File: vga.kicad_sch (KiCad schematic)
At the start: 52 parts

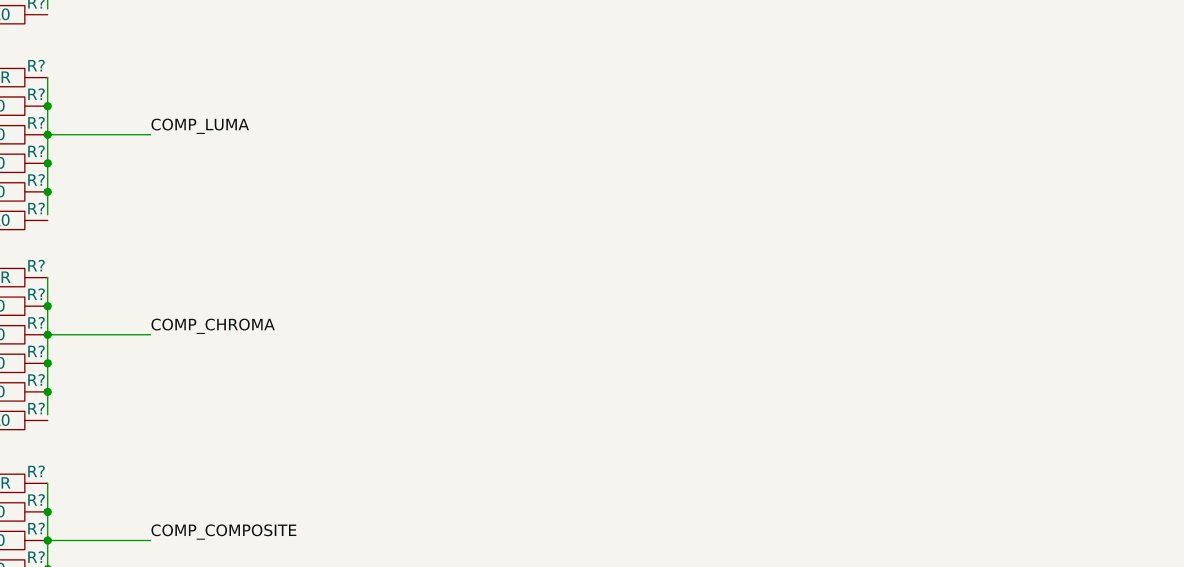
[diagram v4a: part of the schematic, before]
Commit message: add 3.5mm audio jack
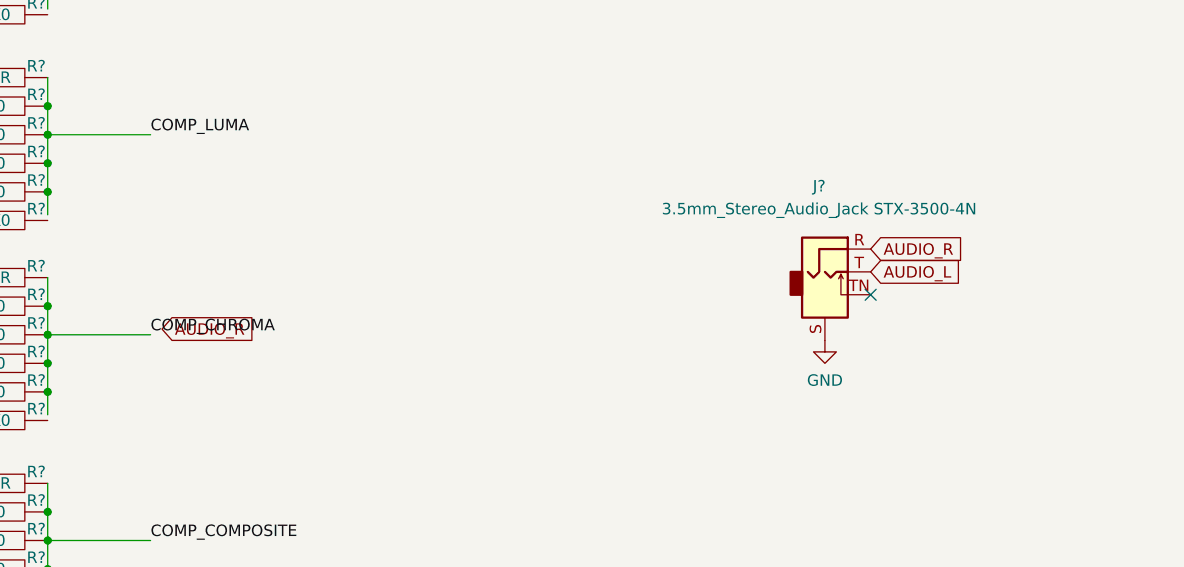
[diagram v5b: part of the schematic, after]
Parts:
- added J?: 3.5mm_Stereo_Audio_Jack STX-3500-4N, Connector_Audio:Jack_3.5mm_CUI_SJ-3524-SMT_Horizontal, symbol 00Project-SDF-60J:3.5mm_Stereo_Audio_Jack STX-3500-4N
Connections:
- net AUDIO_L: now also J?.T
- net AUDIO_R: now also J?.R
- net GND: now also J?.S
- no-connect marks 5 -> 6
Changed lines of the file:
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@@
   (no_connect (at 243.84 120.015))
   (no_connect (at 228.6 54.61))
+  (no_connect (at 139.065 132.715))
   (no_connect (at 243.84 114.935))
   (no_connect (at 228.6 52.07))
@@
     )
   )
+  (global_label "AUDIO_R" (shape input) (at 60.325 136.525 0) (fields_autoplaced)
+    (effects (font (size 1.27 1.27)) (justify left))
+    (property "Intersheet References" "${INTERSHEET_REFS}" (id 0) (at 70.6 136.4456 0)
+      (effects (font (size 1.27 1.27)) (justify left) hide)
+    )
+  )
   (global_label "AUDIO_L1" (shape input) (at 34.925 74.295 180) (fields_autoplaced)
     (effects (font (size 1.27 1.27)) (justify right))
@@
     (property "Intersheet References" "${INTERSHEET_REFS}" (id 0) (at 17.2719 140.2556 0)
       (effects (font (size 1.27 1.27)) (justify right) hide)
+    )
+  )
+  (global_label "AUDIO_R" (shape input) (at 139.065 127.635 0) (fields_autoplaced)
+    (effects (font (size 1.27 1.27)) (justify left))
+    (property "Intersheet References" "${INTERSHEET_REFS}" (id 0) (at 149.34 127.5556 0)
+      (effects (font (size 1.27 1.27)) (justify left) hide)
     )
   )
@@
     (property "Intersheet References" "${INTERSHEET_REFS}" (id 0) (at 165.9526 15.7956 0)
       (effects (font (size 1.27 1.27)) (justify right) hide)
+    )
+  )
+  (global_label "AUDIO_L" (shape input) (at 139.065 130.175 0) (fields_autoplaced)
+    (effects (font (size 1.27 1.27)) (justify left))
+    (property "Intersheet References" "${INTERSHEET_REFS}" (id 0) (at 149.0981 130.0956 0)
+      (effects (font (size 1.27 1.27)) (justify left) hide)
     )
   )
@@
     (pin "2")
   )
+  (symbol (lib_id "power:GND") (at 133.985 137.795 0) (unit 1)
+    (in_bom yes) (on_board yes) (fields_autoplaced)
+    (property "Reference" "#PWR?" (id 0) (at 133.985 144.145 0)
+      (effects (font (size 1.27 1.27)) hide)
+    )
+    (property "Value" "GND" (id 1) (at 133.985 142.24 0))
+    (property "Footprint" "" (id 2) (at 133.985 137.795 0)
+      (effects (font (size 1.27 1.27)) hide)
+    )
+    (property "Datasheet" "" (id 3) (at 133.985 137.795 0)
+      (effects (font (size 1.27 1.27)) hide)
+    )
+    (pin "1")
+  )
   (symbol (lib_id "pspice:R") (at 41.275 160.02 90) (unit 1)
     (in_bom yes) (on_board yes)
@@
     (pin "2")
   )
+  (symbol (lib_id "00Project-SDF-60J:3.5mm_Stereo_Audio_Jack STX-3500-4N") (at 133.985 130.175 0) (unit 1)
+    (in_bom yes) (on_board yes) (fields_autoplaced)
+    (property "Reference" "J?" (id 0) (at 133.35 120.65 0))
+    (property "Value" "3.5mm_Stereo_Audio_Jack STX-3500-4N" (id 1) (at 133.35 123.19 0))
+    (property "Footprint" "Connector_Audio:Jack_3.5mm_CUI_SJ-3524-SMT_Horizontal" (id 2) (at 131.445 117.475 0)
+      (effects (font (size 1.27 1.27)) hide)
+    )
+    (property "Datasheet" "https://www.kycon.com/Pub_Eng_Draw/STX-3500-4N.pdf" (id 3) (at 133.985 120.015 0)
+      (effects (font (size 1.27 1.27)) hide)
+    )
+    (pin "R")
+    (pin "S")
+    (pin "T")
+    (pin "TN")
+  )
   (symbol (lib_id "pspice:R") (at 41.275 95.25 90) (unit 1)

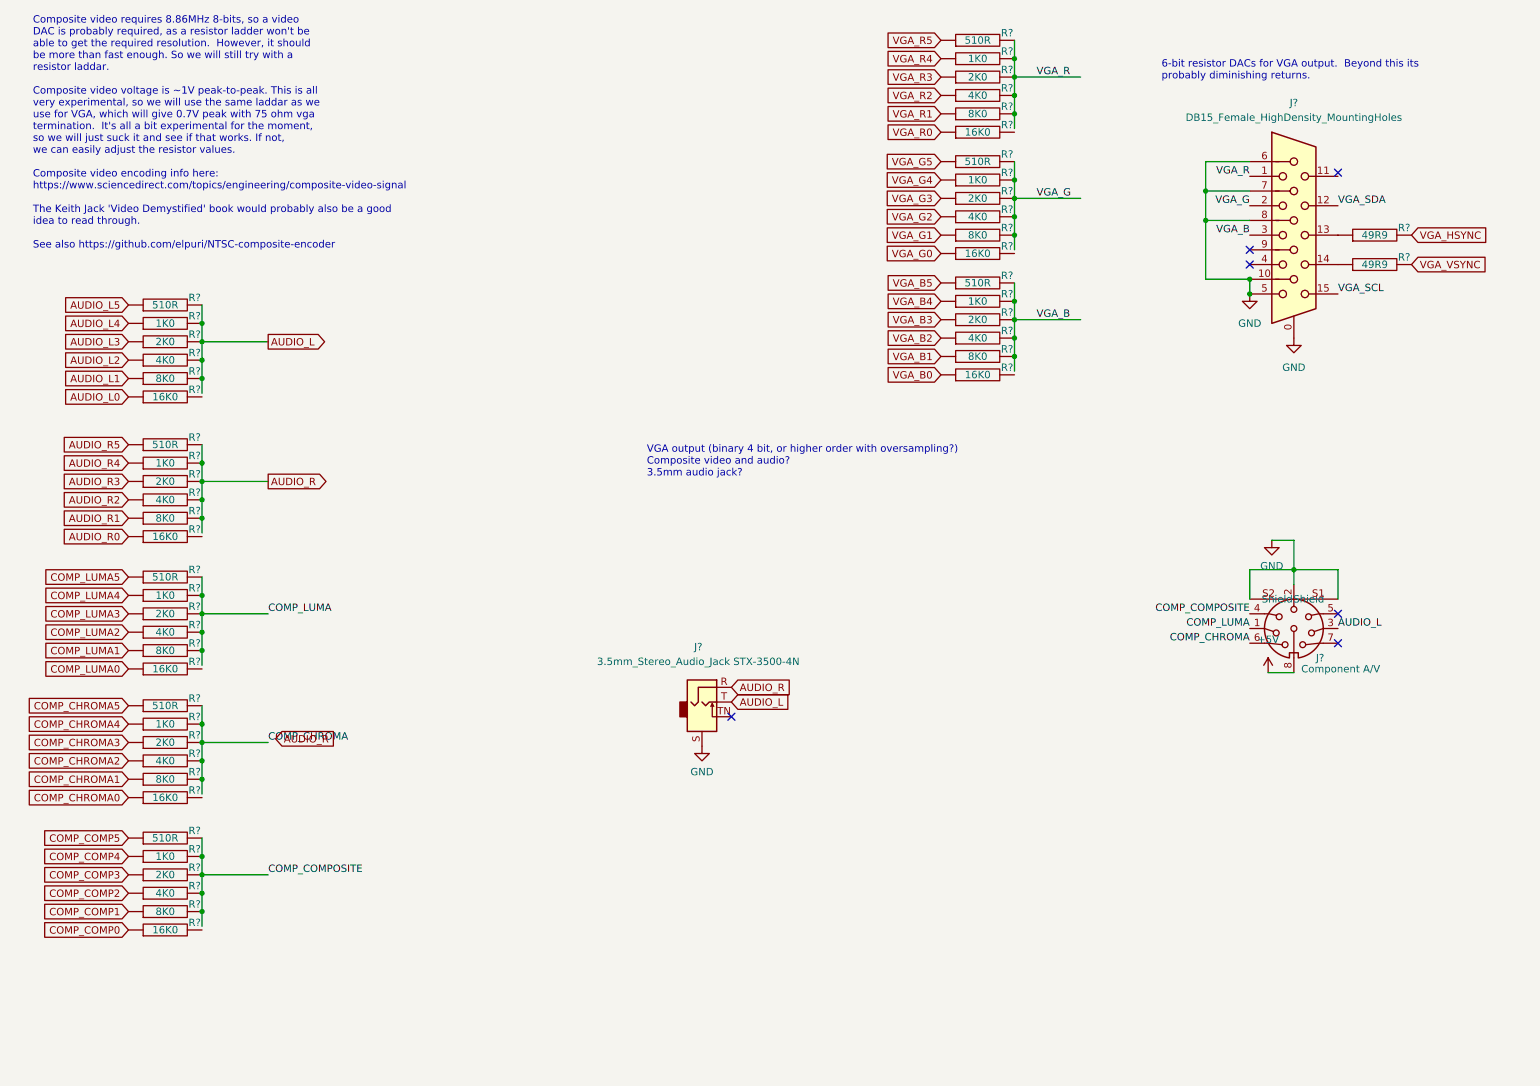
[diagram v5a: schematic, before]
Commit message: add reversable audio header, e.g., for internal speakers + amp
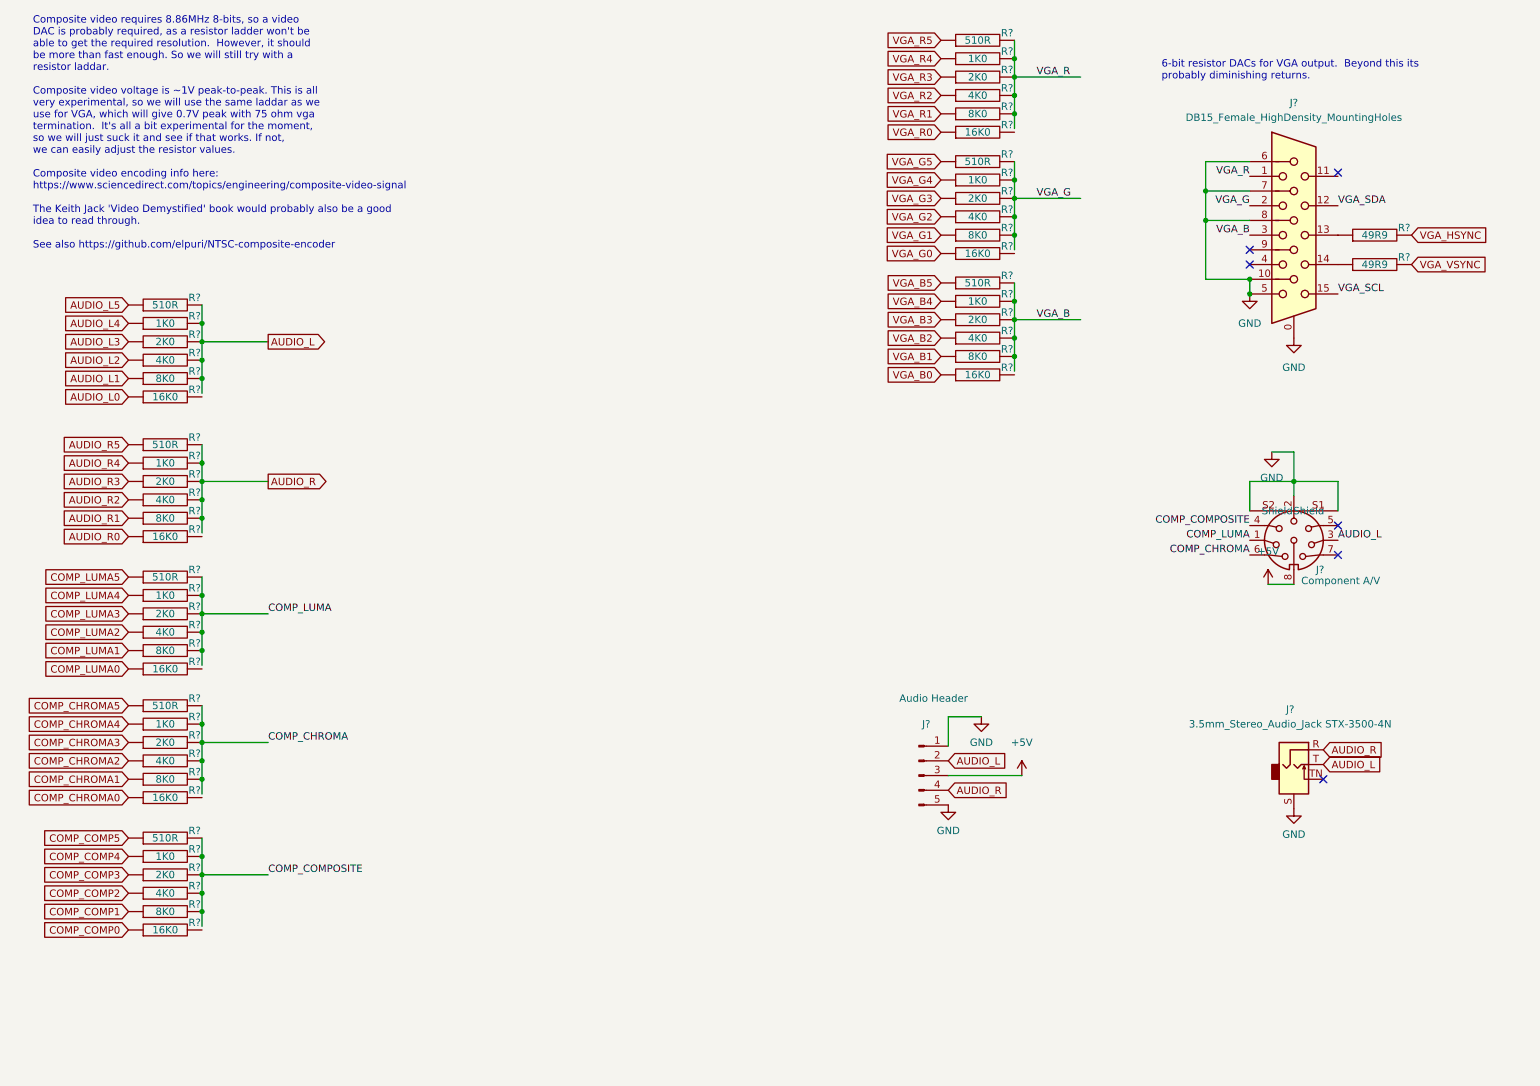
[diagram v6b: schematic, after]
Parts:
- added J?: Audio Header, symbol Connector:Conn_01x05_Male
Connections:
- net +5V: now also J?.3 (Pin_3)
- net AUDIO_L: now also J?.2 (Pin_2)
- net AUDIO_R: now also J?.4 (Pin_4)
- net GND: now also J?.1 (Pin_1), J?.5 (Pin_5)
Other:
- note removed: "VGA output (binary 4 bit, or higher order with oversampling?) Composite video and audio? 3.5mm audio jack?"
- moved on the sheet: J?

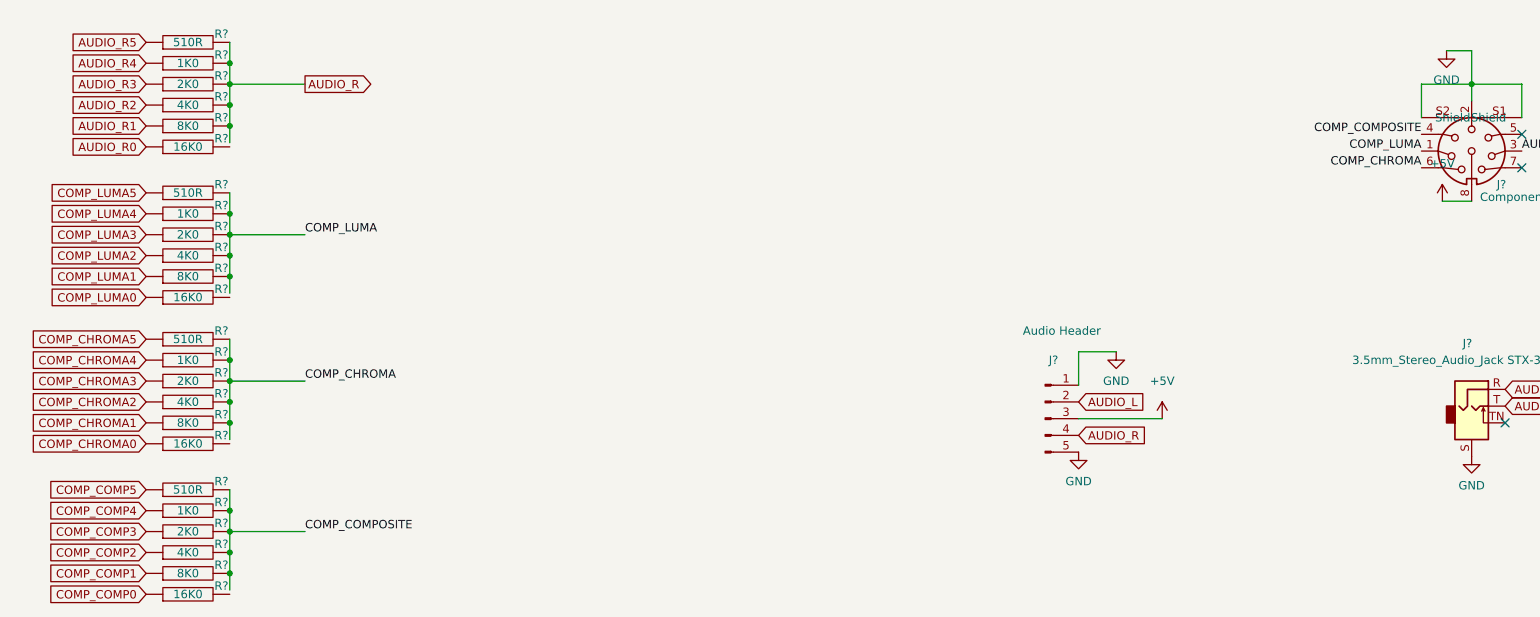
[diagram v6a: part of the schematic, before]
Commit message: plumb all direct FPGA signals.
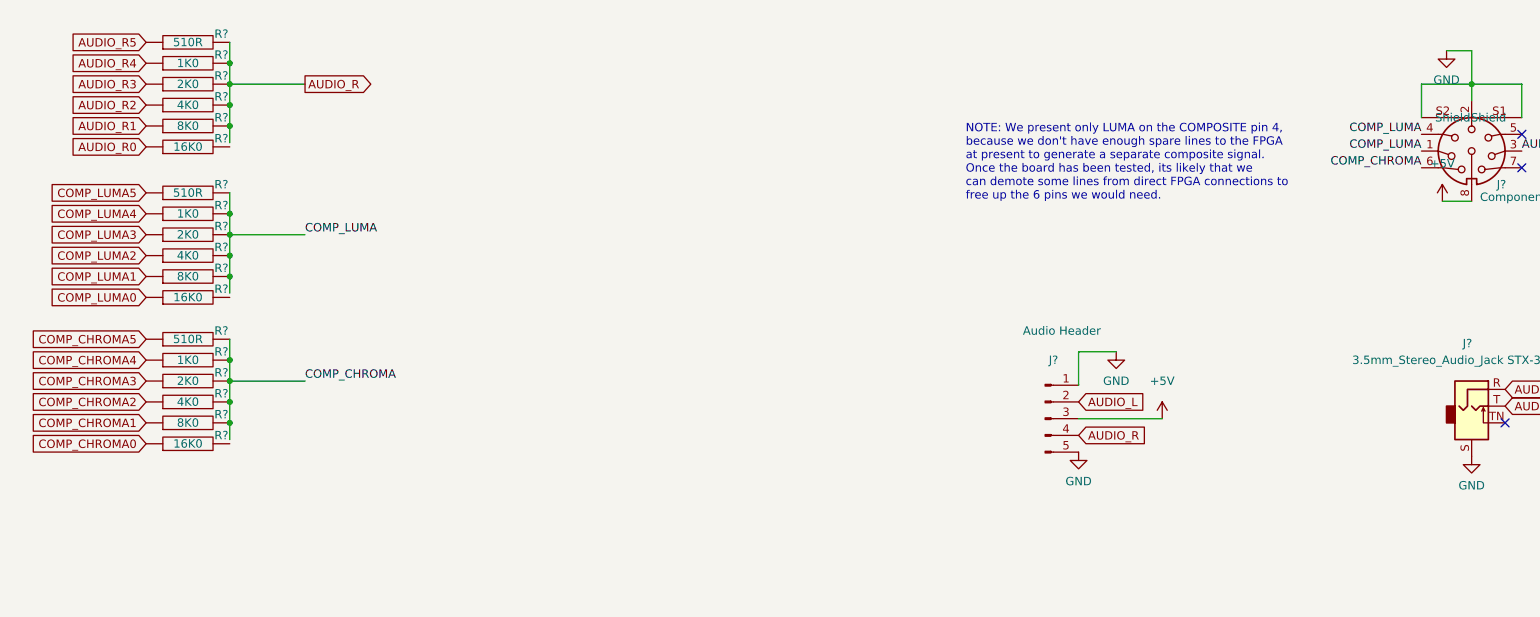
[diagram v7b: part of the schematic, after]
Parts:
- removed R?: 4K0, Resistor_THT:R_Box_L8.4mm_W2.5mm_P5.08mm, symbol pspice:R
- removed R?: 16K0, Resistor_THT:R_Box_L8.4mm_W2.5mm_P5.08mm, symbol pspice:R
- removed R?: 510R, Resistor_THT:R_Box_L8.4mm_W2.5mm_P5.08mm, symbol pspice:R
- removed R?: 8K0, Resistor_THT:R_Box_L8.4mm_W2.5mm_P5.08mm, symbol pspice:R
- removed R?: 2K0, Resistor_THT:R_Box_L8.4mm_W2.5mm_P5.08mm, symbol pspice:R
- removed R?: 1K0, Resistor_THT:R_Box_L8.4mm_W2.5mm_P5.08mm, symbol pspice:R
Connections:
- net COMP_COMPOSITE is gone; now on net COMP_LUMA: J?.4
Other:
- note added: "NOTE: We present only LUMA on the COMPOSITE pin 4, because we don't have enough spare lines to the FPGA at present to generate a separate composite signal. Once the board has been tested, its likely that we can demote some lines from direct FPGA connections to free up the 6 pins we would need."
